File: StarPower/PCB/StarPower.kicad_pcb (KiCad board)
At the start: 2 copper layers, 42 x 14.5 mm, 21 parts, among them SW1 TL3301, U1 ATtiny25-20SSU, U2 SGM809B-SXN3LG, U3 PAM2804AAB010, Y1 32.768 kHz

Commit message: Remove C4 & C5, the load capacitors at the crystal.
The internal capacitance of the ATtinyx5 is enough.
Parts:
- removed C3, C4: C, Capacitor_SMD:C_0805_2012Metric_Pad1.18x1.45mm_HandSolder
- removed the REF** at (112.0, 109.3)
- removed the REF** at (112.9, 108.1)
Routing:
- net GND: track 67.4 -> 57.0 mm
- net /XTAL1: track 6.95 -> 2.50 mm
- net /XTAL2: track 6.75 -> 2.49 mm

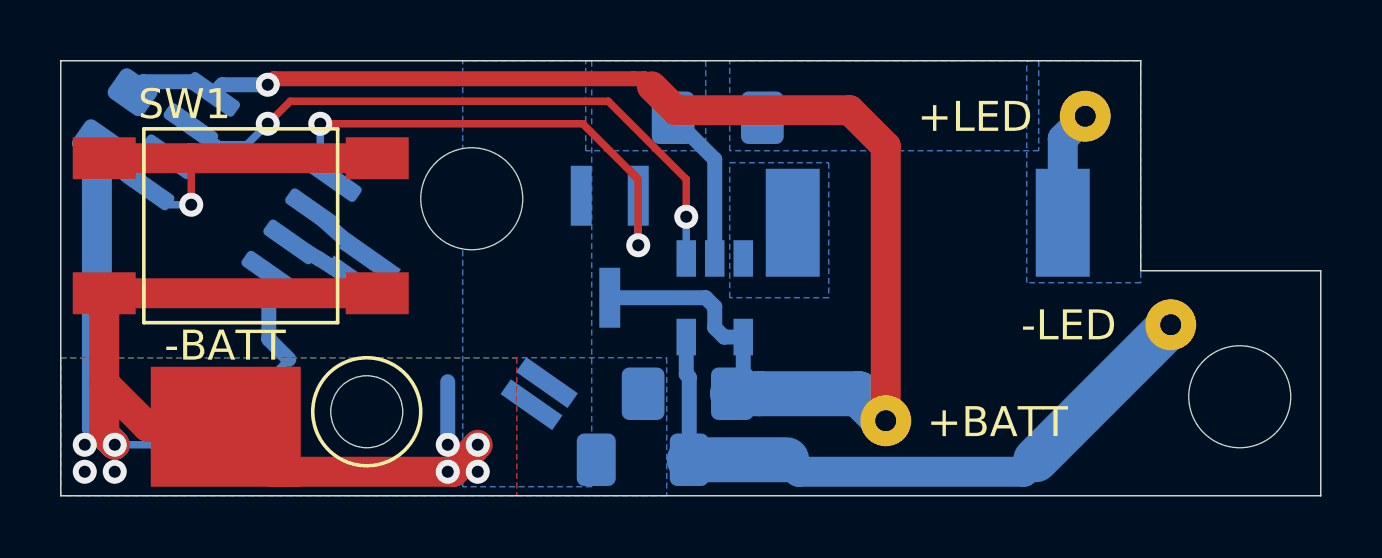
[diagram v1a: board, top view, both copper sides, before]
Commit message: Changed microcontroller footprint of U1, and using the low voltage type now.
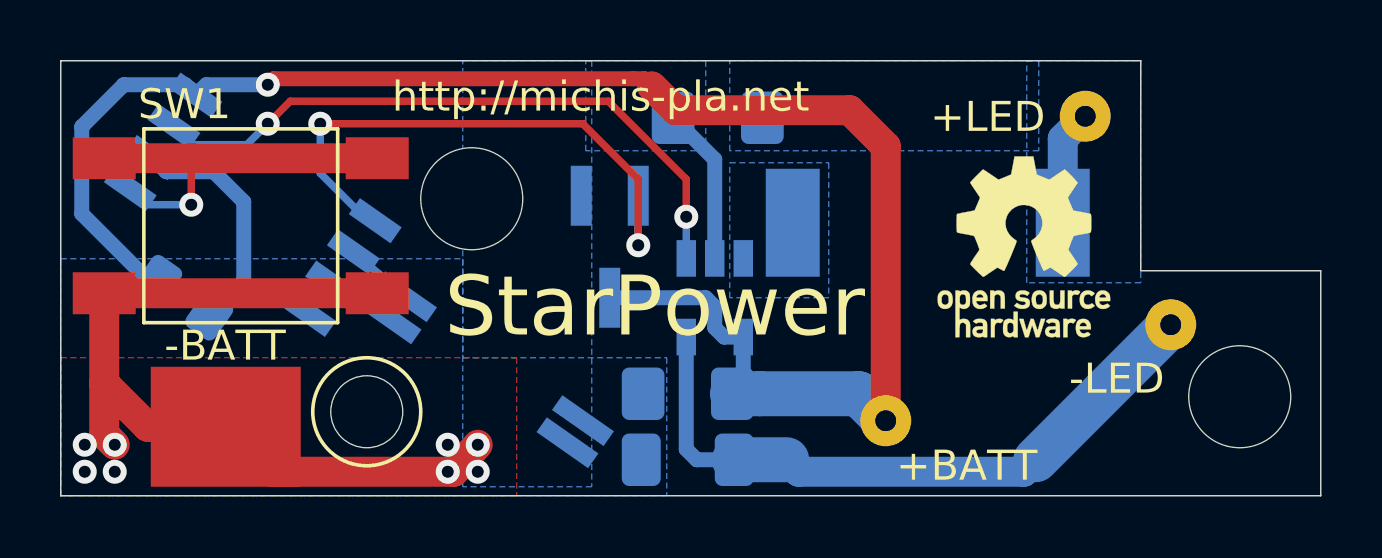
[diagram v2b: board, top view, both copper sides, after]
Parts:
- added REF**: OSHW-Logo_5.7x6mm_SilkScreen, Symbol:OSHW-Logo_5.7x6mm_SilkScreen, F.Cu at (132.1, 106.2)
- U1: value ATtiny25-20SSU -> ATtiny25V-10SU; footprint Package_SO:SOIC-8_3.9x4.9mm_P1.27mm -> Package_SO:SOIJ-8_5.3x5.3mm_P1.27mm
- moved C5 6.43 mm to (104.1, 107.9), turned to 325 degrees
- moved Y1 1.74 mm to (114.2, 110.3)
- moved R1 1.50 mm to (120.9, 113.3)
- moved U1 0.81 mm to (106.4, 104.8)
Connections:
- net Net-(SW1-Pad1) renamed /BUTTON
- U1 pad 6: Net-(U1-Pad6) -> GND
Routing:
- net GND: track 57.0 -> 41.6 mm
- net +BATT: track 48.7 -> 57.2 mm
- net ~RESET: track 17.3 -> 19.4 mm
- net ENABLE: track 21.0 -> 21.6 mm
- net /BUTTON: track 12.4 -> 12.9 mm
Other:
- board text added: "Rev. 22/2"
- board text added: "StarPower"
- board text added: "http://michis-pla.net"
- board text removed: "Rev. 22/1"
